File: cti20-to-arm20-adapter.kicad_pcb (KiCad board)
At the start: 2 copper layers, 12.7 x 30.7 mm, 2 parts, among them J1 Conn_02x10_Odd_Even, J2 Conn_02x10_Odd_Even

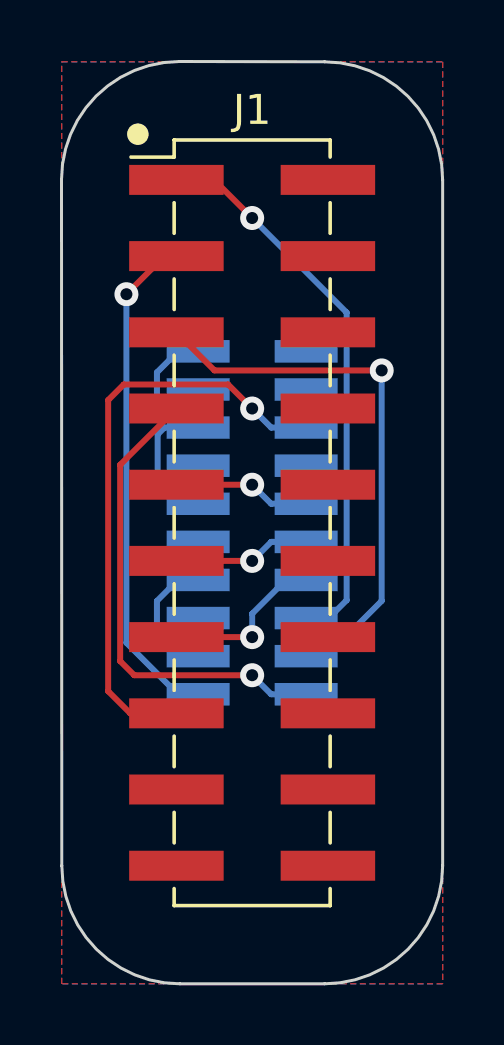
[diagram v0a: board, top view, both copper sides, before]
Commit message: holepunches for gnd plane
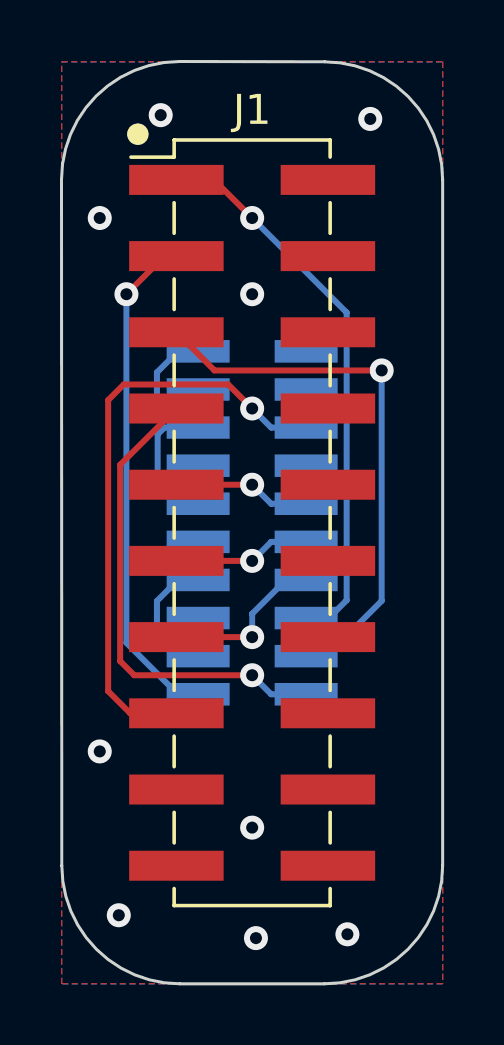
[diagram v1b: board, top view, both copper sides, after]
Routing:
- net GND: vias 0 -> 9
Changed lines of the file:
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@@
   (segment (start 103.697 89.535) (end 101.981 87.819) (width 0.2) (layer "B.Cu") (net 3))
   (segment (start 101.981 87.819) (end 101.981 76.2) (width 0.2) (layer "B.Cu") (net 3))
+  (via (at 106.172 76.2) (size 0.8) (drill 0.4) (layers "F.Cu" "B.Cu") (free) (net 4))
+  (via (at 110.109 70.358) (size 0.8) (drill 0.4) (layers "F.Cu" "B.Cu") (free) (net 4))
+  (via (at 101.727 96.901) (size 0.8) (drill 0.4) (layers "F.Cu" "B.Cu") (free) (net 4))
+  (via (at 109.347 97.536) (size 0.8) (drill 0.4) (layers "F.Cu" "B.Cu") (free) (net 4))
+  (via (at 101.092 91.44) (size 0.8) (drill 0.4) (layers "F.Cu" "B.Cu") (free) (net 4))
+  (via (at 106.172 93.98) (size 0.8) (drill 0.4) (layers "F.Cu" "B.Cu") (free) (net 4))
+  (via (at 106.299 97.663) (size 0.8) (drill 0.4) (layers "F.Cu" "B.Cu") (free) (net 4))
+  (via (at 101.092 73.66) (size 0.8) (drill 0.4) (layers "F.Cu" "B.Cu") (free) (net 4))
+  (via (at 103.124 70.231) (size 0.8) (drill 0.4) (layers "F.Cu" "B.Cu") (free) (net 4))
   (segment (start 103.697 78.105) (end 102.997 78.805) (width 0.2) (layer "B.Cu") (net 4))
   (segment (start 104.372 78.105) (end 103.697 78.105) (width 0.2) (layer "B.Cu") (net 4))

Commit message: update cti connector. layout is not updated
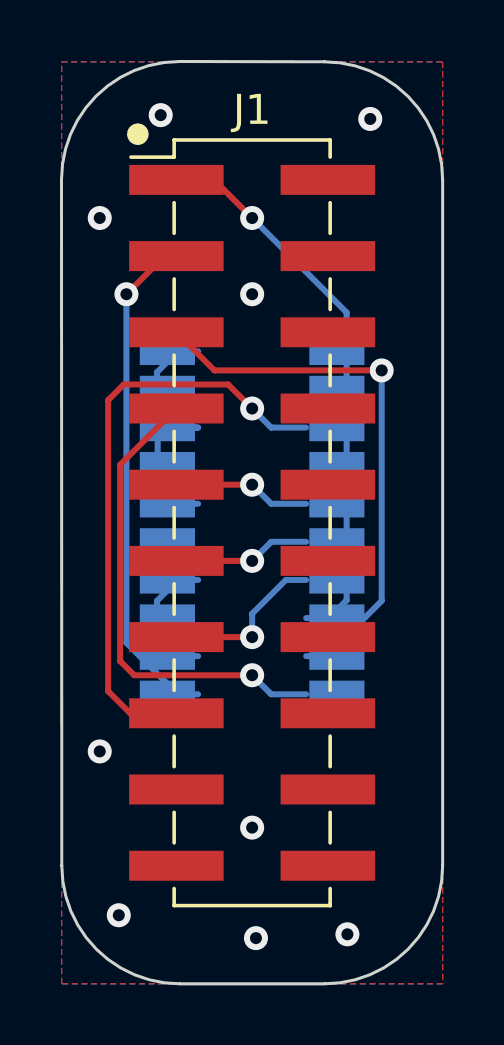
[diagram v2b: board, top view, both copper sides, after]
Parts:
- J2: footprint Connector_PinSocket_1.27mm:PinSocket_2x10_P1.27mm_Vertical_SMD -> RSM-110-02-L-D:SAMTEC_RSM-110-02-L-D
- turned J2 to 90 degrees
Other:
- board text added: "rev 2"
- board text removed: "rev 1"
